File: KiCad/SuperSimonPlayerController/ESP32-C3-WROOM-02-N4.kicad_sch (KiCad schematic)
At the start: 4 parts, among them U1 ESP32-C3-WROOM-02-N4(4MB)

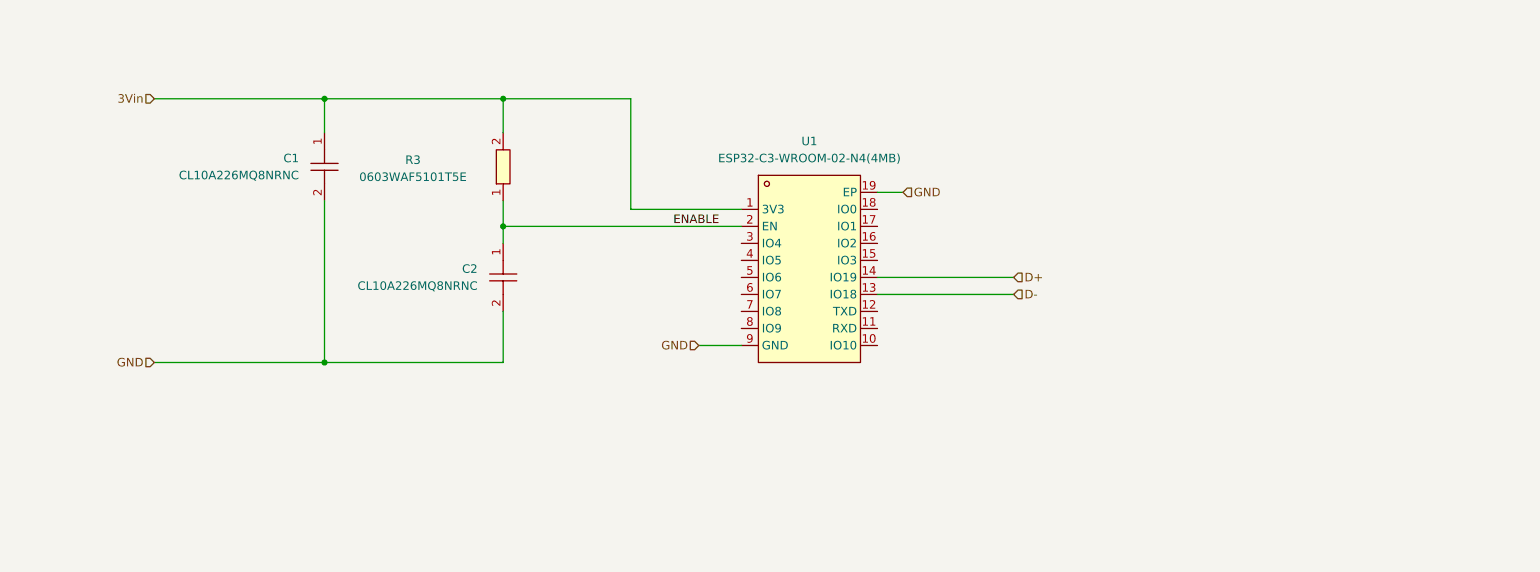
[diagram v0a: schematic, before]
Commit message: Added switches and boot-strapping pull-ups to esp32-c3
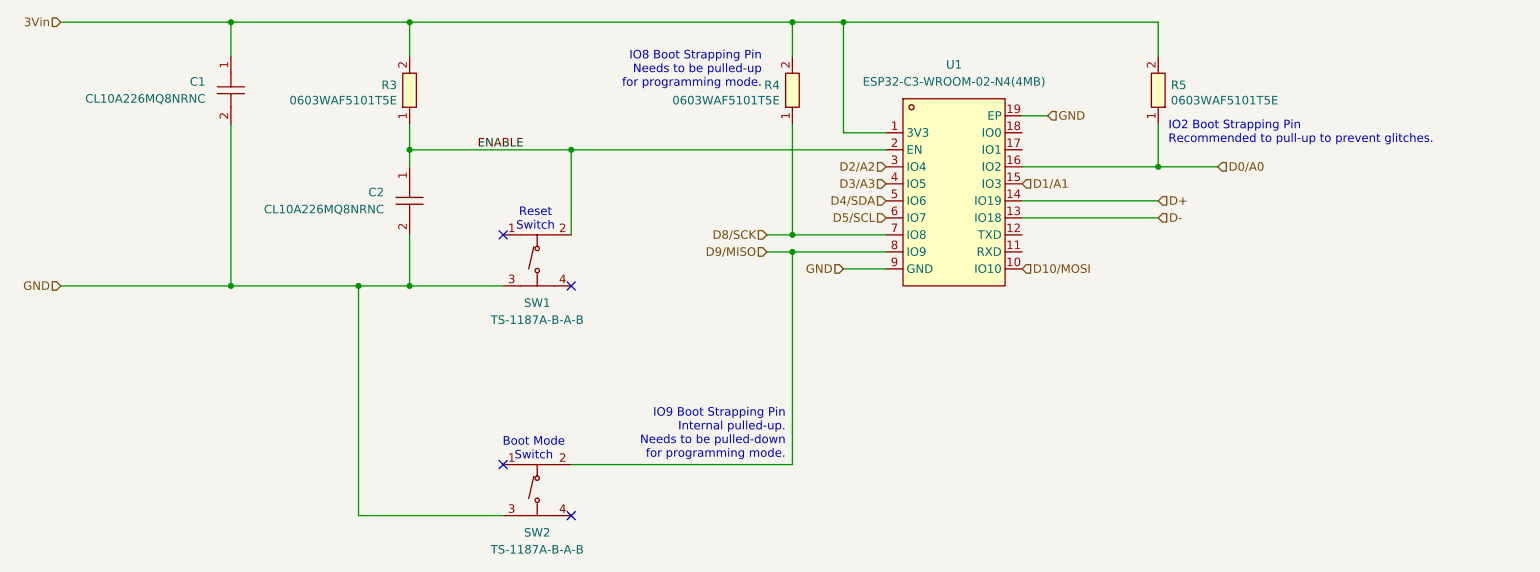
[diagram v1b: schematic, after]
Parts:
- added R4, R5: 0603WAF5101T5E, easyeda2kicad:R0603, symbol easyeda2kicad:0603WAF5101T5E
- added SW1, SW2: TS-1187A-B-A-B, easyeda2kicad:SW-SMD_4P-L5.1-W5.1-P3.70-LS6.5-TL_H1.5, symbol easyeda2kicad:TS-1187A-B-A-B
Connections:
- net 3Vin: now also R4.2, R5.2
- net ENABLE: now also SW1.2
- net GND: now also SW1.3, SW2.3
- net D10/MOSI: now reaches U1.10 (IO10)
- net D1/A1: now reaches U1.15 (IO3)
- net D0/A0: now reaches U1.16 (IO2)
- net D0/A0: now also R5.1
- net D2/A2: now reaches U1.3 (IO4)
- net D3/A3: now reaches U1.4 (IO5)
- net D4/SDA: now reaches U1.5 (IO6)
- net D5/SCL: now reaches U1.6 (IO7)
- net D8/SCK: now reaches U1.7 (IO8)
- net D8/SCK: now also R4.1
- net D9/MISO: now reaches U1.8 (IO9)
- net D9/MISO: now also SW2.2
- no-connect marks 0 -> 4
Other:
- note added: "Boot Mode Switch"
- note added: "IO2 Boot Strapping Pin Recommended to pull-up to prevent glitches."
- note added: "IO8 Boot Strapping Pin Needs to be pulled-up for programming mode."
- note added: "IO9 Boot Strapping Pin Internal pulled-up. Needs to be pulled-down for programming mode."
- note added: "Reset Switch"
- moved on the sheet: C1, C2, R3, U1
